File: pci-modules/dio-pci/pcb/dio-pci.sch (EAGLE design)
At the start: 111 parts, among them Q1 SSM3J328R, U1 4901, U2 7933, U3 ADN4663, U4 ADN4663, U5 ADN4664, U6 PDS1, U7 4901

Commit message: Added some part selections for the pci-dio board.
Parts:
- removed D10, D11, D12, D13, D8, D9: STPS0560Z, jonnew:S-DIODESOD-123
- removed D7: BZT52C7V5, jonnew:Z-DIODE_SOD123
- removed G24, G25, G27: 142-0701, jonnew:COAX_SMA-VERT
- removed POW_SEL: (no value), jonnew:JP3E
- removed Q1: SSM3J328R, jonnew:P-MOSFET_SOT23-GSD
- removed R11: 10k, jonnew:R_0603
- removed R14, R15, R16: 100, jonnew:R_0603
- removed VDD_AUX: (no value), jonnew:JP2E_THRU-HOLE
- added U$3, U$4: HDMI, jonnew:HDMI
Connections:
- removed net +5V0_ISO-PRE: C14.1, L1.1, U6.+VO
- removed net AUX_VDD: L2.1, POW_SEL.2
- removed net N$18: G25.1, R14.2
- removed net N$19: G27.1, R15.2
- removed net N$2: G24.1, R16.2
- removed net N$3: D7.C, POW_SEL.3, Q1.S
- removed net N$6: D7.A, Q1.G, R11.2
- removed net N$7: Q1.D, VDD_AUX.1
- new net N$9: C11.1, C12.1, L1.2, U1.EN, U1.IN
- net +3V3: no longer D10.C, D12.C, D8.C
- net +3V6: no longer POW_TP.2
- net +5V0: now also C14.1, L1.1, L2.1, U6.+VO; no longer C11.1, C12.1, L1.2, U1.EN, U1.IN
- net 12V_FPGA: no longer POW_SEL.1
- net G24: no longer D8.A, D9.C, R16.1
- net G25: no longer D10.A, D11.C, R14.1
- net G27: no longer D12.A, D13.C, R15.1
- net GND: no longer C20.2, C21.2, C22.2, C24.2, D11.A, D13.A, D9.A, G24.2, G25.2, G27.2, R11.1, R13.2, U7.EP, U7.GND, VDD_AUX.2
- net GND_ISO: now also C20.2, C21.2, C22.2, C24.2, R13.2, U7.EP, U7.GND
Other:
- note added: "12V-TO-5V ISOLATED DC-DC TODO: Beefier with better isolation"
- note added: "3.6V regulator for RHD TODO: Each RHD has a regulator"
- note added: "Isolated 3.3V reg."
- note added: "TODO: More IO and optional 50 Ohm termination"
- note removed: "12V-TO-5V ISOLATED DC-DC"
- note removed: "3.3V reg. for RHD side supply"
- note removed: "3.6V regulator for RHD"
- note removed: "schottky diodes for input protection"
- moved on the sheet: A, B, C1, C10, C11, C12, C13, C14, C15, C16, C17, C18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

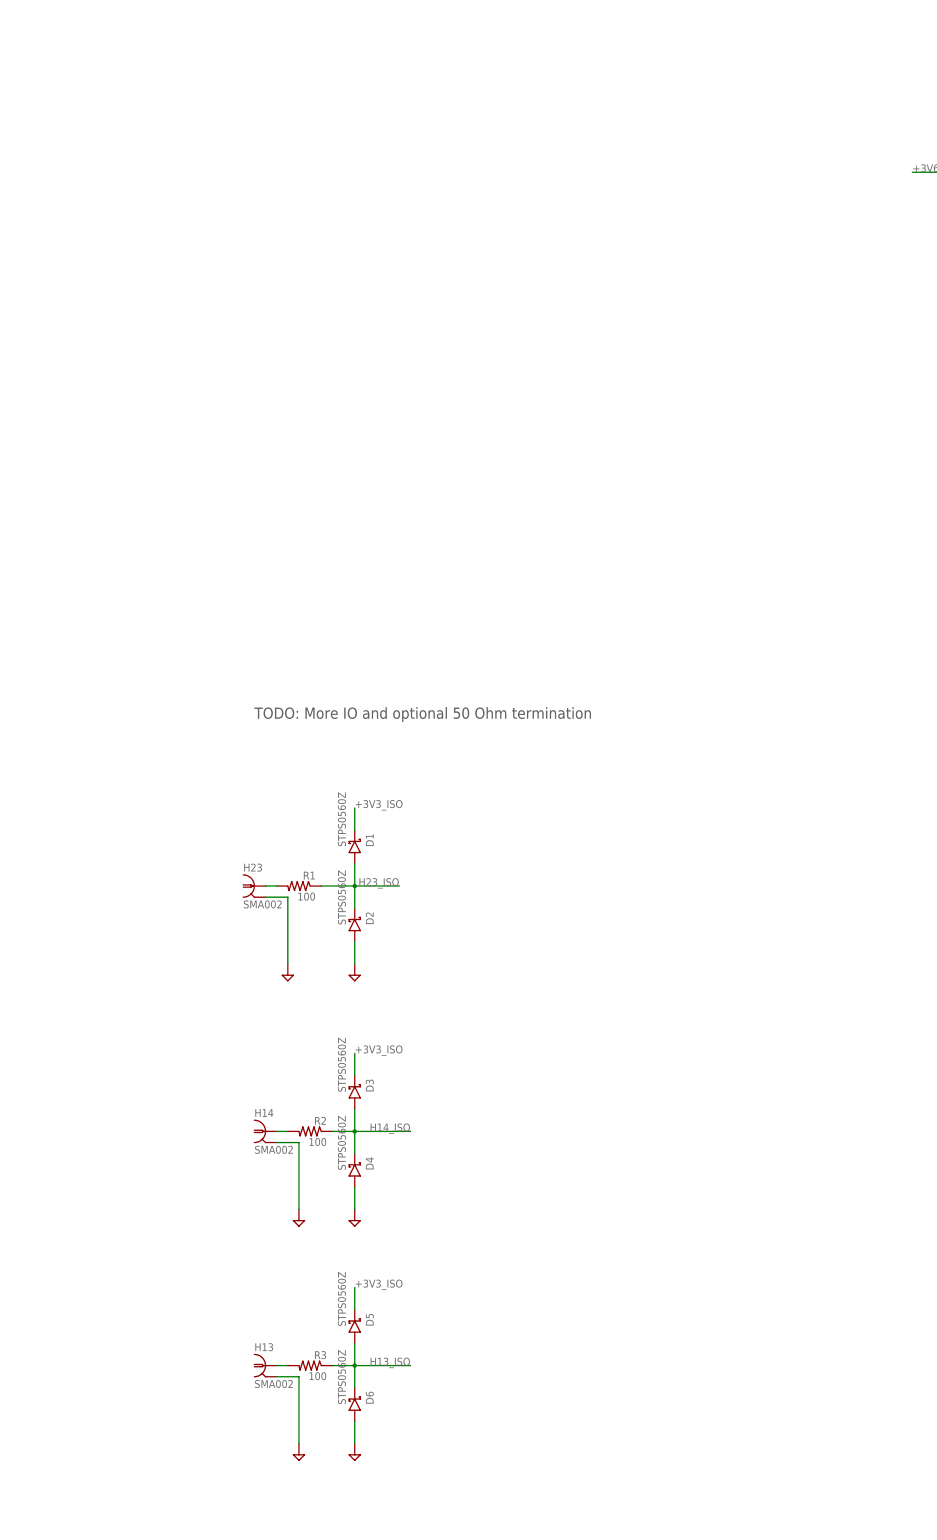
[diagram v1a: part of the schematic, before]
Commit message: Isolated DIO input circuit design on dio-pic card
- Replace current limit resistors with fast polyfuse with I_trip <
  schottky I_max sustained
- Optional 50 Ohm termination on input SMAs
- TTL Logic-level tolerant line driver on output SMAs
- Programable logic level on input SMAs. Still needs DAC on isolated
  side to set bias voltages
- I really want to replace omnetics with HDMI connectors. Having
  omnetics on a PC chasis seems very wrong because they are made of
  cheese.
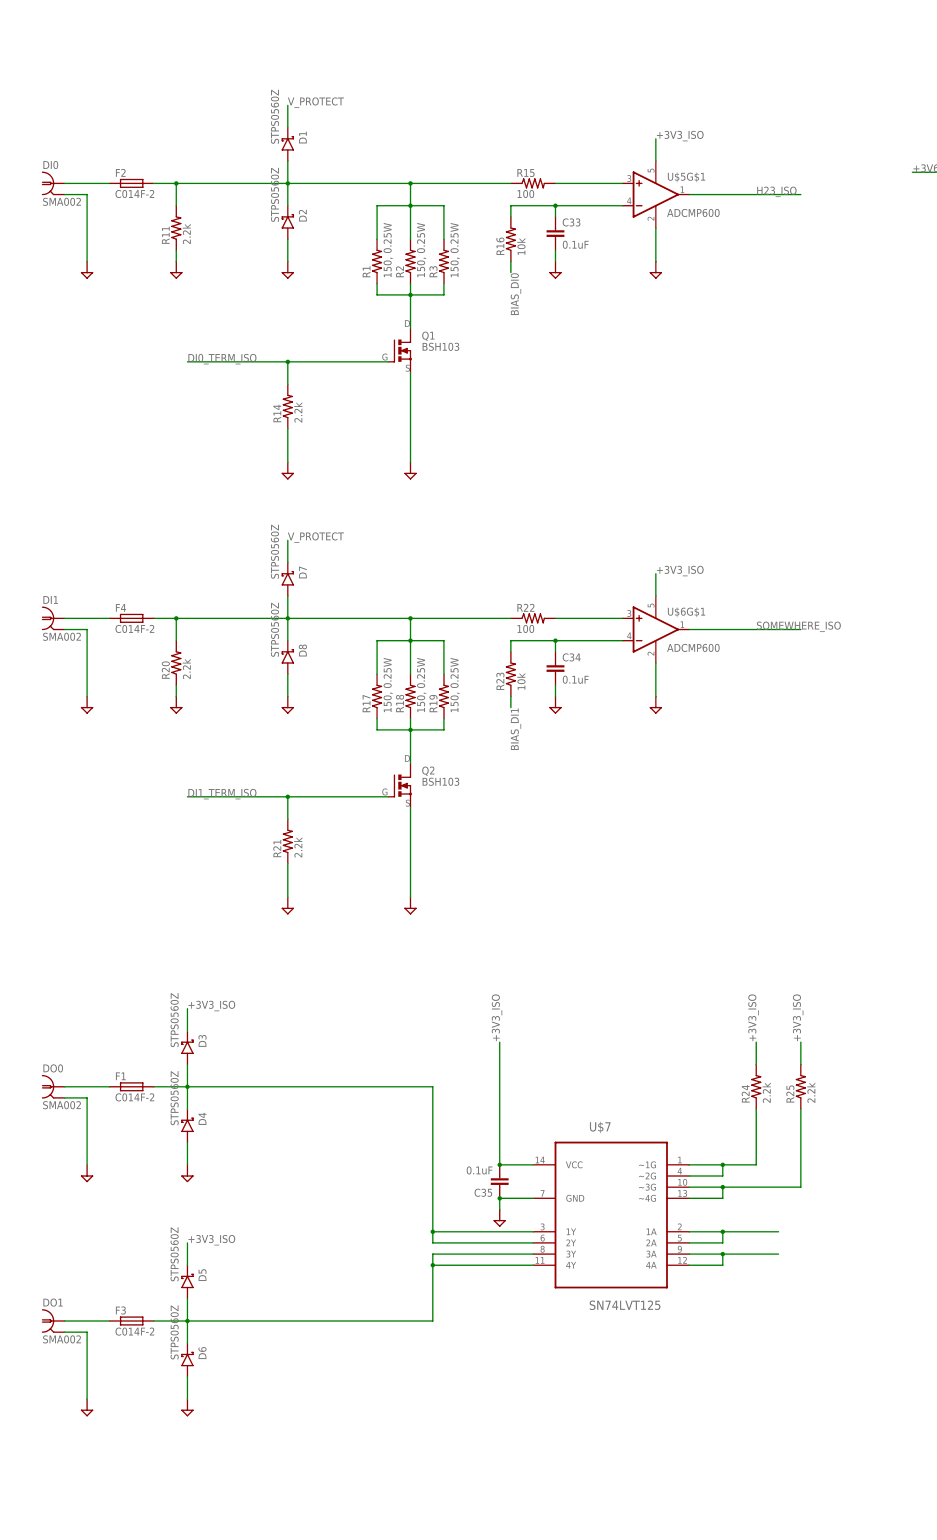
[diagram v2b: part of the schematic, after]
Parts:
- removed H13, H14, H23: SMA002, jonnew:COAX_CONREVSMA002-G
- added C33, C34: 0.1uF, jonnew:C_0603
- added C35: 0.1uF, RHD2000_eval_board:C_0603
- added D7, D8: STPS0560Z, jonnew:S-DIODESOD-123
- added DI0, DI1, DO0, DO1: SMA002, jonnew:COAX_CONREVSMA002-G
- added F1, F2, F3, F4: C014F-2, jonnew:FUSE_1812
- added Q1, Q2: BSH103, jonnew:N-MOSFET_SOT23-GSD
- added R11, R14, R20, R21, R24, R25: 2.2k, jonnew:R_0603
- added R15, R22: 100, jonnew:R_0603
- added R16, R23: 10k, jonnew:R_0603
- added R17, R18, R19: 150, 0.25W, jonnew:R_1206
- added U$5, U$6: ADCMP600, jonnew:COMPARITOR_ADCMP600
- added U$7: SN74LVT125, jonnew:QUAD-LINE-DRIVER_SOIC
- R1, R2, R3: value 100 -> 150, 0.25W; device jonnew:R_0603 -> jonnew:R_1206
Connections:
- new net $N1: D7.A, D8.C, F4.2, R17.2, R18.2, R19.2, R20.2, R22.1
- new net $N101: D3.A, D4.C, F1.2, U$7.1Y, U$7.2Y
- new net $N102: D5.A, D6.C, F3.2, U$7.3Y, U$7.4Y
- new net $N3: D1.A, D2.C, F2.2, R1.2, R11.2, R15.1, R2.2, R3.2
- new net BIAS_DI0: R16.1
- new net BIAS_DI1: R23.1
- new net DI0_TERM_ISO: Q1.G, R14.2
- new net DI1_TERM_ISO: Q2.G, R21.2
- new net N$18: C33.1, R16.2, U$5G$1.-IN
- new net N$19: R22.2, U$6G$1.+IN
- new net N$2: Q1.D, R1.1, R2.1, R3.1
- new net N$20: C34.1, R23.2, U$6G$1.-IN
- new net N$24: R24.1, U$7.~1G, U$7.~2G
- new net N$25: R25.1, U$7.~3G, U$7.~4G
- new net N$3: R15.2, U$5G$1.+IN
- new net N$6: DI1.1, F4.1
- new net N$7: Q2.D, R17.1, R18.1, R19.1
- new net SOMEWHERE_ISO: U$6G$1.OUT
- new net V_PROTECT: D1.C, D7.C
- net +3V3_ISO: now also C35.2, R24.2, R25.2, U$5G$2.V+, U$6G$2.V+, U$7.VCC; no longer D1.C
- net GND_ISO: now also C33.2, C34.2, C35.1, D8.A, DI0.2, DI1.2, DO0.2, DO1.2, Q1.S, Q2.S, R11.1, R14.1, R20.1, R21.1, U$5G$2.V-, U$6G$2.V-, U$7.GND; no longer H13.2, H14.2, H23.2
- net H13_ISO: now also U$7.3A, U$7.4A; no longer D5.A, D6.C, R3.1
- net H14_ISO: now also U$7.1A, U$7.2A; no longer D3.A, D4.C, R2.1
- net H23_ISO: now also U$5G$1.OUT; no longer D1.A, D2.C, R1.1
- net N$11: now also DI0.1, F2.1; no longer H23.1, R1.2
- net N$14: now also DO0.1, F1.1; no longer H14.1, R2.2
- net N$17: now also DO1.1, F3.1; no longer H13.1, R3.2
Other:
- note removed: "TODO: More IO and optional 50 Ohm termination"
- moved on the sheet: D1, D2, D3, D4, D5, D6, R1, R2, R3

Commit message: Designed protection network for dio-pci card
- TTL, LVTTL, CMOS logic level compatible
- Resistant to incorrect logic levels and low impedance DC or AC sources
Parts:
- removed C14: 10uF, jonnew:C_1206
- removed U2: 7933, jonnew:TPS79333
- added C36, C37: 0.1uF, jonnew:C_0603
- added D9: KDZ4.3B, jonnew:Z-DIODE_SOD123
- added IC1: AZ1117CH-3.3, jonnew:317EMP
- added L3, L4: MPZ1608, jonnew:L_0603
- added L5: 82103C, jonnew:L_1206
- added R26, R27: 2.2k, jonnew:R_0603
- added TP8: +5V0, jonnew:TPTP06R
- C13: value 1.0uF -> 10uF; device RHD2000_eval_board:C_0805 -> jonnew:C_1206
- C6: value 10nF -> 0.1uF; device RHD2000_eval_board:C_0603 -> jonnew:C_0603
- U6: value PDS1 -> MEV3S1209SC; device jonnew:PDS1 -> jonnew:DC-DC-CONVERTER_MEV3
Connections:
- removed net N$97: C6.1, U2.NR
- new net +9V0_ISO: L1.1, L2.1, L3.1, R26.2, R27.2, U6.+VO
- new net N$21: C13.1, IC1.VO, L3.2
- new net N$22: IC1.VI, L4.1
- new net N$23: L5.2, U6.VIN
- net +3V3_ISO: now also C36.1, C37.1, L4.2; no longer D3.C, D5.C, U2.OUT
- net +5V0: no longer C13.1, C14.1, L1.1, L2.1, U2.EN, U2.IN, U6.+VO
- net 12V_FPGA: now also L5.1; no longer U6.VIN
- net GND_ISO: now also C36.2, C37.2, C6.1, D9.A, IC1.ADJ; no longer C14.2, C6.2, U2.GND
- net V_PROTECT: now also C6.2, D3.C, D5.C, D9.C, R26.1, R27.1, TP8.TP
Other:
- note added: "12V-TO-9V ISOLATED DC-DC"
- note added: "TODO: 1. Correct package on 82103C filter inductor 2. DAC to set LL bias on comparitors"
- note added: "V_PROTECT ~4.6V"
- note removed: "12V-TO-5V ISOLATED DC-DC TODO: Beefier with better isolation"
- moved on the sheet: C13, C19, C3, C6, PWR_ISO1, R7
